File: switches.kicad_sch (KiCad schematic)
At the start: 128 parts, among them SW10 SW_Push, SW11 SW_Push, SW14 SW_Push, SW15 SW_Push, SW16 SW_Push, SW18 SW_Push, SW20 SW_Push, SW21 SW_Push, SW22 SW_Push, SW23 SW_Push, SW24 SW_Push, SW25 SW_Push, SW26 SW_Push, SW27 SW_Push, SW28 SW_Push, SW29 SW_Push, SW3 SW_Push, SW30 SW_Push, SW31 SW_Push, SW32 SW_Push, SW35 SW_Push, SW36 SW_Push, SW37 SW_Push, SW38 SW_Push, SW39 SW_Push, SW40 SW_Push, SW41 SW_Push, SW42 SW_Push, SW43 SW_Push, SW44 SW_Push, SW45 SW_Push, SW46 SW_Push, SW47 SW_Push, SW48 SW_Push, SW49 SW_Push, SW5 SW_Push, SW50 SW_Push, SW51 SW_Push, SW52 SW_Push, SW53 SW_Push, SW54 SW_Push, SW56 SW_Push, SW58 SW_Push, SW59 SW_Push, SW60 SW_Push, SW61 SW_Push, SW62 SW_Push, SW65 SW_Push, SW66 SW_Push, SW67 SW_Push, SW68 SW_Push, SW69 SW_Push, SW7 SW_Push, SW71 SW_Push, SW73 SW_Push, SW74 SW_Push, SW75 SW_Push, SW76 SW_Push, SW78 SW_Push, SW79 SW_Push, SW80 SW_Push, SW82 SW_Push, SW84 SW_Push, SW86 SW_Push, SW9 SW_Push

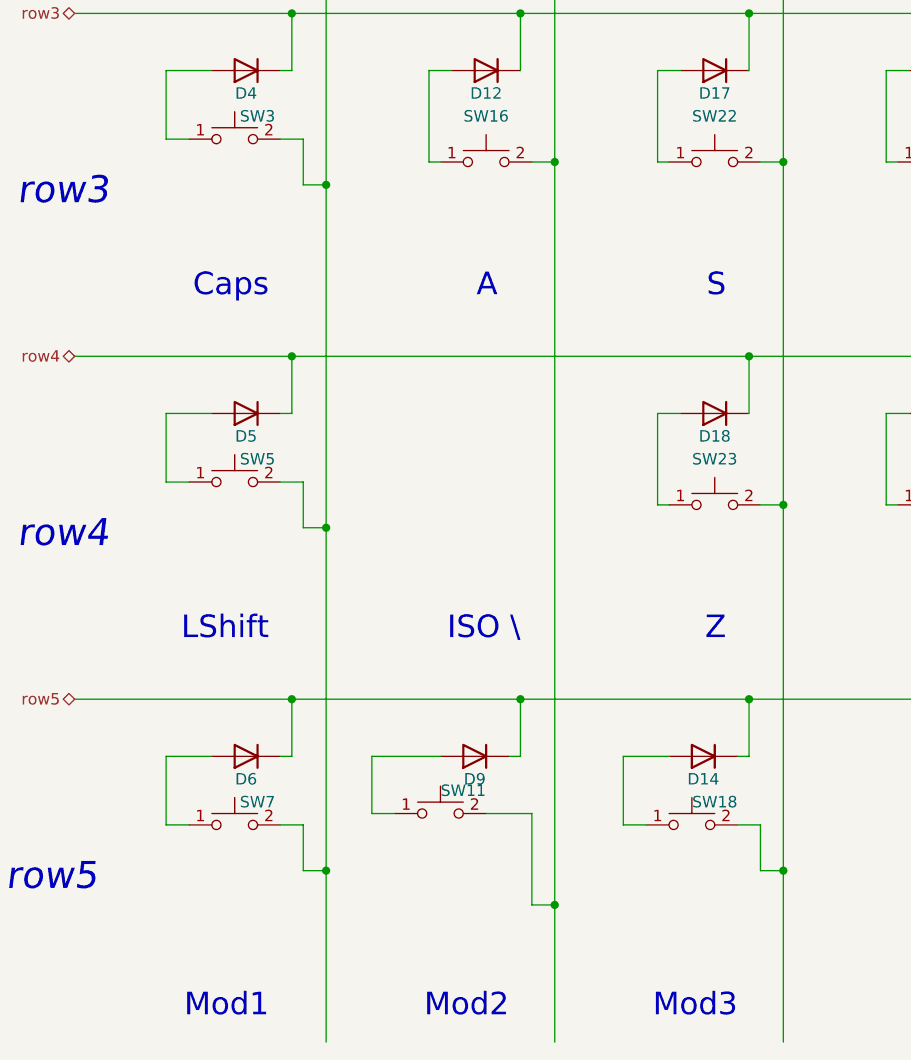
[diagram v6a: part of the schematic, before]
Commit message: add iso layout "iso /" key
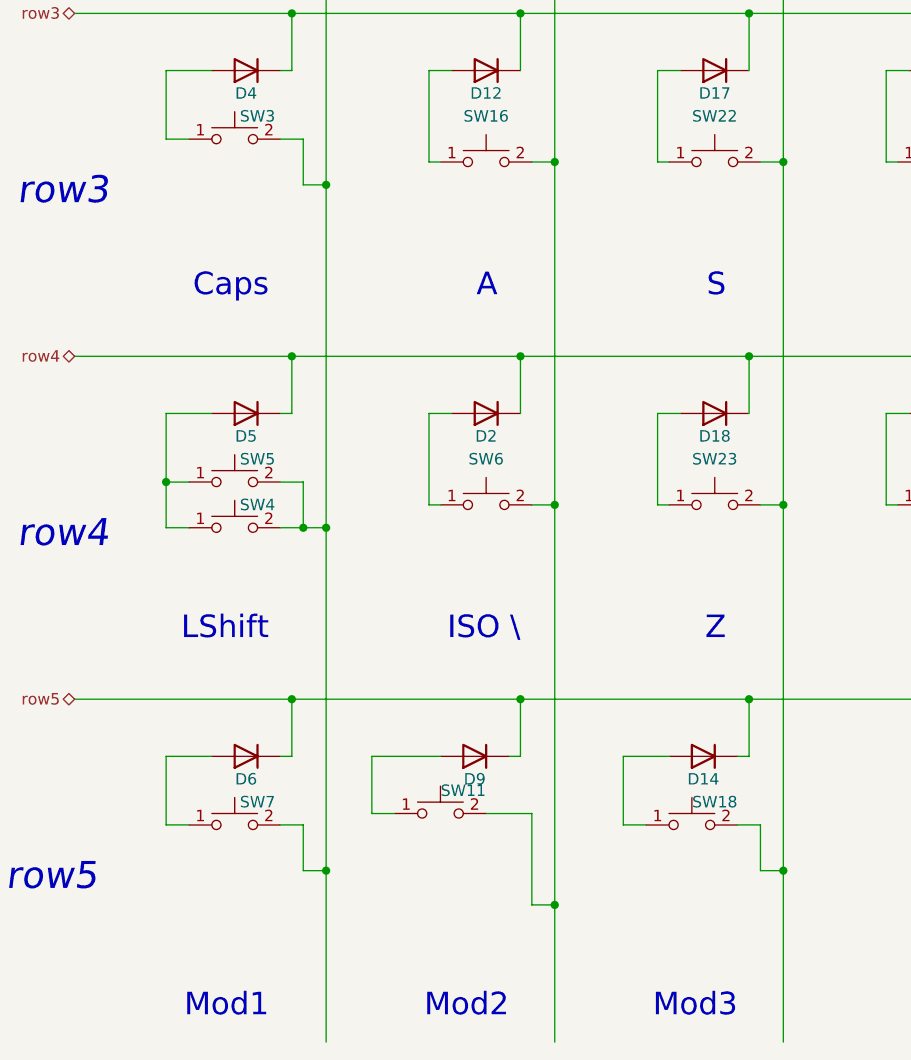
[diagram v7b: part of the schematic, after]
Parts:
- added D2: 1N4148, Diode_SMD:D_0805_2012Metric, symbol Diode:1N4148
- added SW4, SW6: SW_Push, keyswitches:Kailh_socket_MX, symbol Switch:SW_Push
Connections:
- net col1: now also SW4.2
- net col2: now also SW6.2
- net row4: now also D2.1 (K)
- net at D5.2 (A), SW5.1: now also SW4.1
- new net: D2.2 (A), SW6.1
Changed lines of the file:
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@@
   (junction (at 252.73 54.61) (diameter 0) (color 0 0 0 0)
   )
+  (junction (at 78.74 185.42) (diameter 0) (color 0 0 0 0)
+  )
   (junction (at 278.13 54.61) (diameter 0) (color 0 0 0 0)
   )
@@
   (junction (at 281.94 147.32) (diameter 0) (color 0 0 0 0)
   )
+  (junction (at 35.56 182.88) (diameter 0) (color 0 0 0 0)
+  )
   (junction (at 53.34 149.86) (diameter 0) (color 0 0 0 0)
   )
@@
   (junction (at 78.74 71.12) (diameter 0) (color 0 0 0 0)
   )
+  (junction (at 74.93 168.91) (diameter 0) (color 0 0 0 0)
+  )
   (junction (at 332.74 229.87) (diameter 0) (color 0 0 0 0)
   )
+  (junction (at 50.8 187.96) (diameter 0) (color 0 0 0 0)
+  )
   (junction (at 151.13 168.91) (diameter 0) (color 0 0 0 0)
   )
@@
     (stroke (width 0) (type default) (color 0 0 0 0))
   )
+  (wire (pts (xy 74.93 168.91) (xy 100.33 168.91))
+    (stroke (width 0) (type default) (color 0 0 0 0))
+  )
   (wire (pts (xy 245.11 175.26) (xy 242.57 175.26))
     (stroke (width 0) (type default) (color 0 0 0 0))
@@
     (stroke (width 0) (type default) (color 0 0 0 0))
   )
+  (wire (pts (xy 38.1 187.96) (xy 35.56 187.96))
+    (stroke (width 0) (type default) (color 0 0 0 0))
+  )
   (wire (pts (xy 278.13 130.81) (xy 303.53 130.81))
     (stroke (width 0) (type default) (color 0 0 0 0))
@@
     (stroke (width 0) (type default) (color 0 0 0 0))
   )
+  (wire (pts (xy 64.77 185.42) (xy 66.04 185.42))
+    (stroke (width 0) (type default) (color 0 0 0 0))
+  )
   (wire (pts (xy 303.53 130.81) (xy 328.93 130.81))
     (stroke (width 0) (type default) (color 0 0 0 0))
@@
     (stroke (width 0) (type default) (color 0 0 0 0))
   )
+  (wire (pts (xy 35.56 187.96) (xy 35.56 182.88))
+    (stroke (width 0) (type default) (color 0 0 0 0))
+  )
   (wire (pts (xy 354.33 54.61) (xy 379.73 54.61))
     (stroke (width 0) (type default) (color 0 0 0 0))
@@
     (stroke (width 0) (type default) (color 0 0 0 0))
   )
+  (wire (pts (xy 67.31 175.26) (xy 64.77 175.26))
+    (stroke (width 0) (type default) (color 0 0 0 0))
+  )
   (wire (pts (xy 125.73 130.81) (xy 151.13 130.81))
     (stroke (width 0) (type default) (color 0 0 0 0))
@@
     (stroke (width 0) (type default) (color 0 0 0 0))
   )
-  (wire (pts (xy 78.74 147.32) (xy 78.74 229.87))
+  (wire (pts (xy 78.74 147.32) (xy 78.74 185.42))
     (stroke (width 0) (type default) (color 0 0 0 0))
   )
@@
     (stroke (width 0) (type default) (color 0 0 0 0))
   )
+  (wire (pts (xy 64.77 175.26) (xy 64.77 185.42))
+    (stroke (width 0) (type default) (color 0 0 0 0))
+  )
   (wire (pts (xy 118.11 99.06) (xy 115.57 99.06))
     (stroke (width 0) (type default) (color 0 0 0 0))
   )
+  (wire (pts (xy 48.26 187.96) (xy 50.8 187.96))
+    (stroke (width 0) (type default) (color 0 0 0 0))
+  )
   (wire (pts (xy 140.97 175.26) (xy 140.97 185.42))
     (stroke (width 0) (type default) (color 0 0 0 0))
@@
     (stroke (width 0) (type default) (color 0 0 0 0))
   )
+  (wire (pts (xy 74.93 168.91) (xy 74.93 175.26))
+    (stroke (width 0) (type default) (color 0 0 0 0))
+  )
   (wire (pts (xy 76.2 219.71) (xy 76.2 229.87))
     (stroke (width 0) (type default) (color 0 0 0 0))
@@
     (stroke (width 0) (type default) (color 0 0 0 0))
   )
+  (wire (pts (xy 76.2 185.42) (xy 78.74 185.42))
+    (stroke (width 0) (type default) (color 0 0 0 0))
+  )
   (wire (pts (xy 328.93 168.91) (xy 354.33 168.91))
     (stroke (width 0) (type default) (color 0 0 0 0))
@@
     (stroke (width 0) (type default) (color 0 0 0 0))
   )
-  (wire (pts (xy 49.53 168.91) (xy 100.33 168.91))
+  (wire (pts (xy 49.53 168.91) (xy 74.93 168.91))
     (stroke (width 0) (type default) (color 0 0 0 0))
   )
@@
     (stroke (width 0) (type default) (color 0 0 0 0))
   )
+  (wire (pts (xy 78.74 185.42) (xy 78.74 229.87))
+    (stroke (width 0) (type default) (color 0 0 0 0))
+  )
   (wire (pts (xy 53.34 226.06) (xy 53.34 245.11))
     (stroke (width 0) (type default) (color 0 0 0 0))
@@
     (pin "2")
   )
+  (symbol (lib_id "Switch:SW_Push") (at 43.18 187.96 0) (unit 1)
+    (in_bom yes) (on_board yes)
+    (property "Reference" "SW4" (id 0) (at 45.72 185.42 0))
+    (property "Value" "SW_Push" (id 1) (at 43.18 182.88 0)
+      (effects (font (size 1.27 1.27)) hide)
+    )
+    (property "Footprint" "keyswitches:Kailh_socket_MX" (id 2) (at 43.18 182.88 0)
+      (effects (font (size 1.27 1.27)) hide)
+    )
+    (property "Datasheet" "~" (id 3) (at 43.18 182.88 0)
+      (effects (font (size 1.27 1.27)) hide)
+    )
+    (pin "1")
+    (pin "2")
+  )
   (symbol (lib_id "Switch:SW_Push") (at 372.11 67.31 0) (unit 1)
     (in_bom yes) (on_board yes)
@@
     (pin "2")
   )
+  (symbol (lib_id "Switch:SW_Push") (at 71.12 185.42 0) (unit 1)
+    (in_bom yes) (on_board yes)
+    (property "Reference" "SW6" (id 0) (at 71.12 180.34 0))
+    (property "Value" "SW_Push" (id 1) (at 71.12 180.34 0)
+      (effects (font (size 1.27 1.27)) hide)
+    )
+    (property "Footprint" "keyswitches:Kailh_socket_MX" (id 2) (at 71.12 180.34 0)
+      (effects (font (size 1.27 1.27)) hide)
+    )
+    (property "Datasheet" "~" (id 3) (at 71.12 180.34 0)
+      (effects (font (size 1.27 1.27)) hide)
+    )
+    (pin "1")
+    (pin "2")
+  )
   (symbol (lib_id "Switch:SW_Push") (at 193.04 219.71 0) (unit 1)
     (in_bom yes) (on_board yes)
@@
       (effects (font (size 1.27 1.27)) hide)
     )
+    (pin "1")
+    (pin "2")
+  )
+  (symbol (lib_id "Diode:1N4148") (at 71.12 175.26 180) (unit 1)
+    (in_bom yes) (on_board yes)
+    (property "Reference" "D2" (id 0) (at 71.12 177.8 0))
+    (property "Value" "1N4148" (id 1) (at 71.12 179.07 0)
+      (effects (font (size 1.27 1.27)) hide)
+    )
+    (property "Footprint" "Diode_SMD:D_0805_2012Metric" (id 2) (at 71.12 170.815 0)
+      (effects (font (size 1.27 1.27)) hide)
+    )
+    (property "Datasheet" "https://assets.nexperia.com/documents/data-sheet/1N4148_1N4448.pdf" (id 3) (at 71.12 175.26 0)
+      (effects (font (size 1.27 1.27)) hide)
+    )

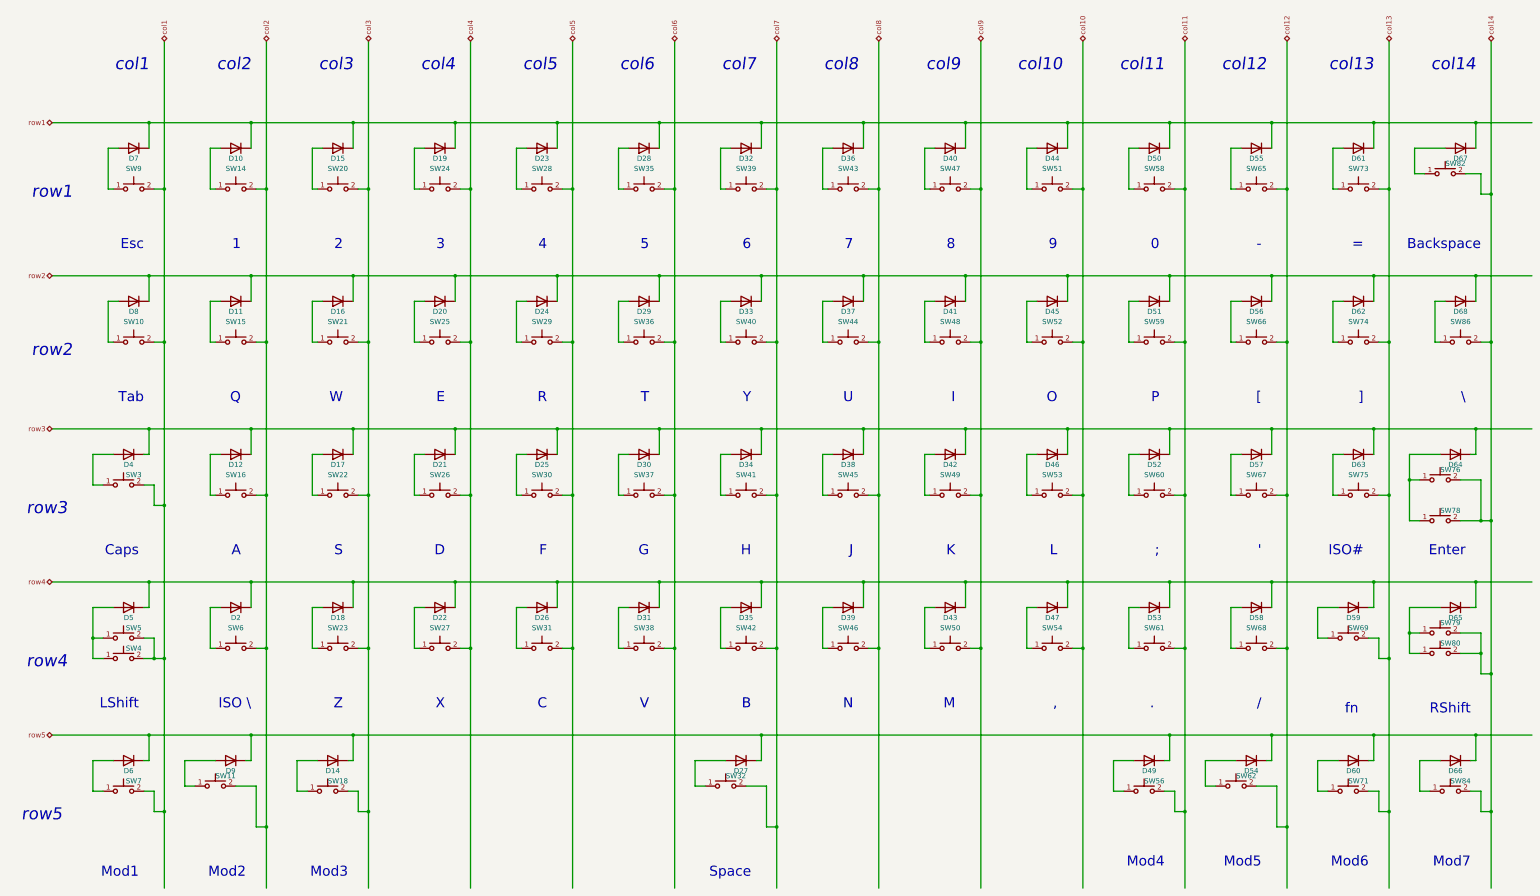
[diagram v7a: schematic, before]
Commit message: remove ISO layout
* iso layout fork to cattle60 project
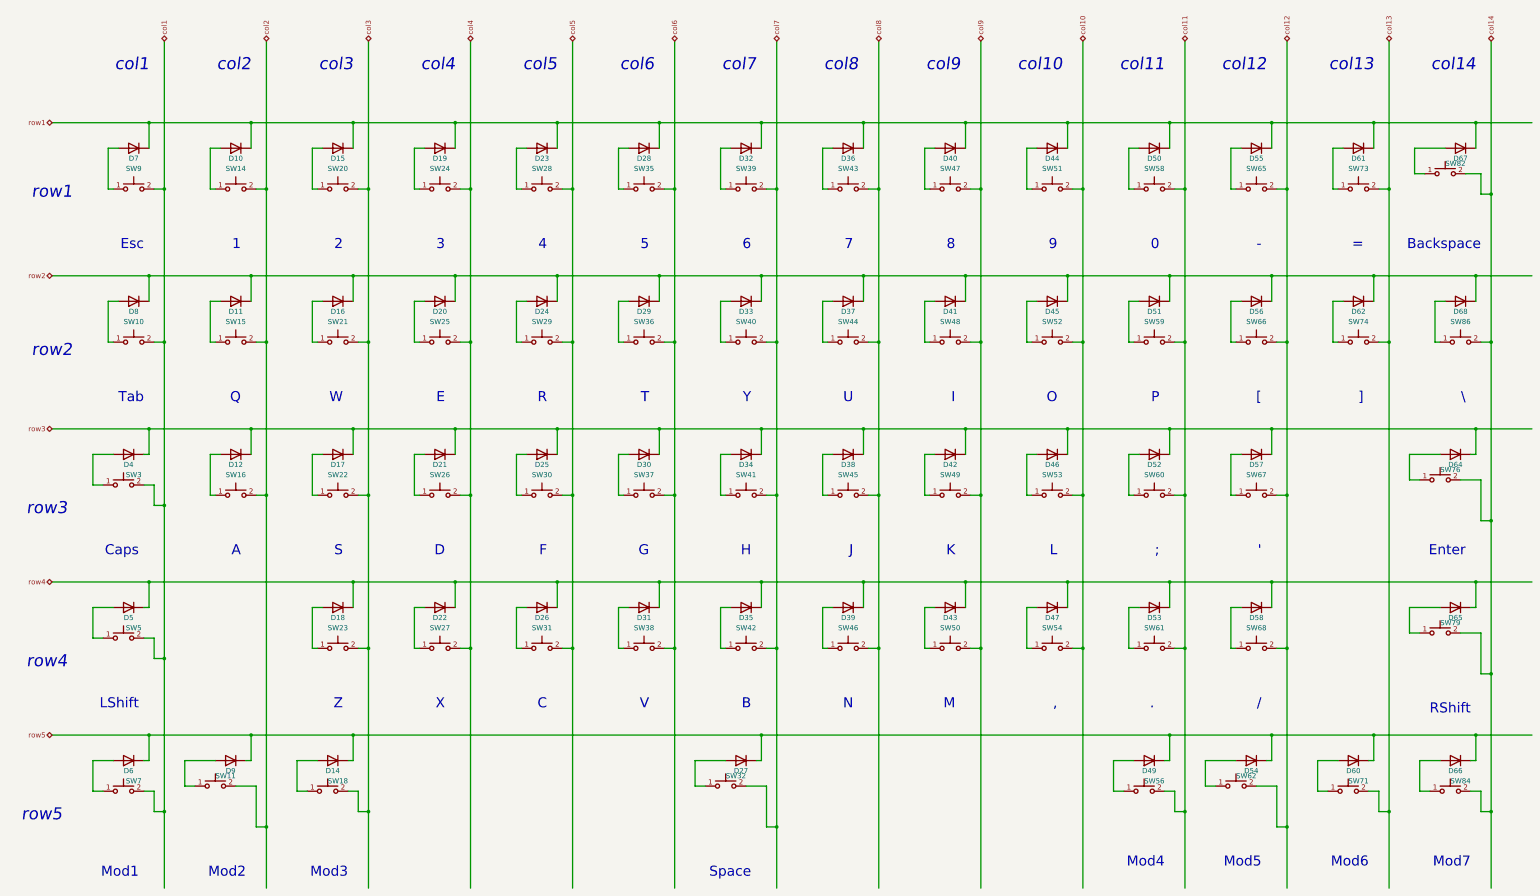
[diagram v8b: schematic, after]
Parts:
- removed D2, D59, D63: 1N4148, Diode_SMD:D_0805_2012Metric, symbol Diode:1N4148
- removed SW4, SW6, SW69, SW75, SW78, SW80: SW_Push, keyswitches:Kailh_socket_MX, symbol Switch:SW_Push
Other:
- note removed: "ISO \"
- note removed: "ISO#"
- note removed: "fn"
